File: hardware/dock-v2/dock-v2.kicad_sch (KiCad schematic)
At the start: 0 parts

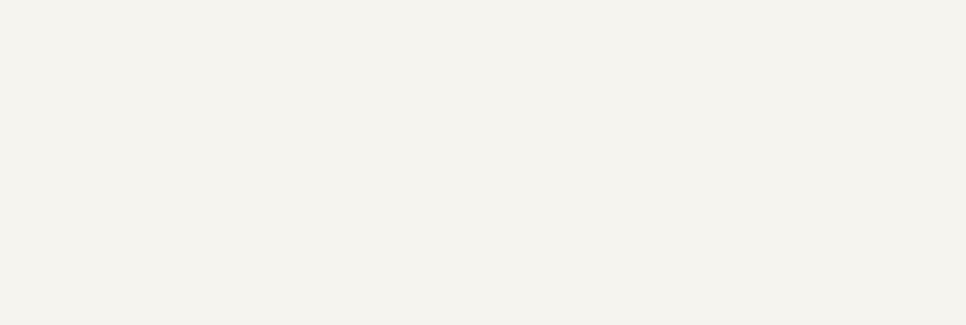
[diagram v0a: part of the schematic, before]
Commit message: Dock v2: six M3 mounting holes, U102 CFG1/PG tracks joined, SWD headers in the model
- H1-H6 (MountingHole_3.2mm_M3, unplated) added to the root schematic and placed:
  back (146,39)/(212,39) beside the USB-C ports, sides (133,58)/(225,58),
  front (160,131)/(200,131) either side of the pogo; symmetric about x = 179-180,
  clear of the ESP32 antenna
- R101/R102 tracks ended 1 mm short of U102 pins 9/10: joined
- J401 (SWD A) and J501 (SWD B) added to the connection model and docs

DRC: 0 violations, 0 unconnected, 0 parity issues. ERC: 1 old warning.

Co-Authored-By: Claude Opus 5.5 <noreply@anthropic.com>
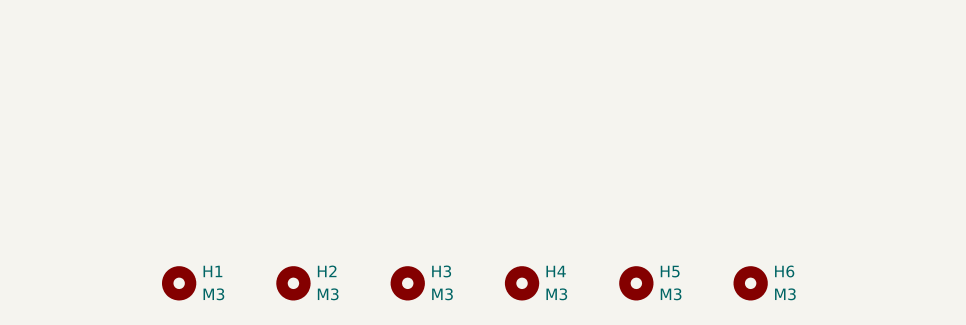
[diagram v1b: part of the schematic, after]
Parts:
- added H1, H2, H3, H4, H5, H6: M3, MountingHole:MountingHole_3.2mm_M3, symbol Mechanical:MountingHole

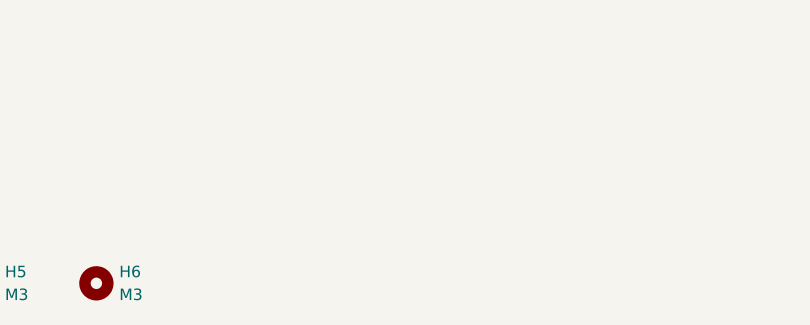
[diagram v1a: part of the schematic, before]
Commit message: Dock v2: extra mounting holes around the USB-C ports (user's work), H7-H10 given own symbols
The four added holes were copies of H5 (same reference and schematic link);
renamed H7-H10 with their own MountingHole symbols on the root sheet.
DRC: 0 violations, 0 unconnected, 0 parity issues.

Co-Authored-By: Claude Opus 5.5 <noreply@anthropic.com>
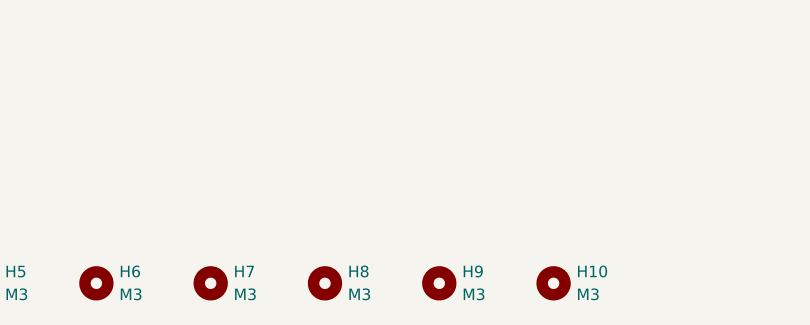
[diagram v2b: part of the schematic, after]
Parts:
- added H10, H7, H8, H9: M3, MountingHole:MountingHole_3.2mm_M3, symbol Mechanical:MountingHole
